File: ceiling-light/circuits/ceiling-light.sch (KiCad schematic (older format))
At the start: 55 parts, among them J1 Screw_Terminal_01x03, J2 Screw_Terminal_01x02, P1 ESProg_Mating_Header, Q1 IRF840, Q2 IRF840, Q3 KSP44, SW1 SW_Push, SW2 SW_Push, U1 TMP36xS, U2 FL51xxMX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

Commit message: schematic work
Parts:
- added Q? (x2): IRF840, Package_TO_SOT_SMD:TO-263-2_TabPin1, symbol Transistor_FET:IRF740
- added R17: 1M, Resistor_SMD:R_1210_3225Metric_Pad1.42x2.65mm_HandSolder, symbol Device:R_Small
- added R?: 10K, Resistor_SMD:R_1210_3225Metric_Pad1.42x2.65mm_HandSolder, symbol Device:R
- added U?: 4N35, Package_DIP:DIP-6_W7.62mm, symbol Isolator:4N35
- R8: value 2M2 -> 1M
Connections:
- net GND: now also U4.3, Q?.3 (S), Q?.3 (S), R?.2
- net at C3.1, D1.2 (A), J1.1 (Pin_1)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: now also C2.2, R17.2; no longer C2.1, R8.2
- net at F1.1, L2.1, Q1.2 (D)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: now also C2.1; no longer C2.2
- net at U6.37 (IO23): now also R12.2, U4.4; no longer U4.3
- new net: R17.1, R8.2
- new net: Q?.1 (G), Q?.1 (G), R?.1, U?.4
- new net +12V: U?.5
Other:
- note added: "!! MAINS VOLTAGE | 230VAC | NOT ISOLATED !!"
- note removed: "!! MAINS VOLTAGE | 230VAC !!"
- moved on the sheet: C1, C12, C13, C15, C2, C4, C6, D1, D2, L1, Q1, Q2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

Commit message: new design
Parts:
- removed C12: 4µ7, Capacitor_SMD:C_1206_3216Metric_Pad1.42x1.75mm_HandSolder, symbol Device:CP_Small
- removed C13: 0.1µ, Capacitor_SMD:C_1206_3216Metric_Pad1.42x1.75mm_HandSolder, symbol Device:CP_Small
- removed C15: 10µ, Capacitor_SMD:C_1210_3225Metric_Pad1.42x2.65mm_HandSolder, symbol Device:CP_Small
- removed D2: WS2812B, LED_SMD:LED_WS2812B_PLCC4_5.0x5.0mm_P3.2mm, symbol LED:WS2812B
- removed D3: LED, symbol Device:LED
- removed D4: D_Bridge_+-AA, Diode_THT_slimc:DB107-BP, symbol Device:D_Bridge_+-AA
- removed Q? (x2): IRF840, Package_TO_SOT_SMD:TO-263-2_TabPin1, symbol Transistor_FET:IRF740
- removed R14, R15: 1K, Resistor_SMD:R_1210_3225Metric_Pad1.42x2.65mm_HandSolder, symbol Device:R_Small
- removed R16: 10K, Resistor_SMD:R_1210_3225Metric_Pad1.42x2.65mm_HandSolder, symbol Device:R_Small
- removed R9: xx, symbol Device:R
- removed R?: 10K, Resistor_SMD:R_1210_3225Metric_Pad1.42x2.65mm_HandSolder, symbol Device:R
- removed U1: TMP36xS, Package_TO_SOT_SMD:SOT-23-5_HandSoldering, symbol Sensor_Temperature:TMP36xS
- removed U5: DAC081C081CIMK, Package_TO_SOT_SMD:SOT-23-6_Handsoldering, symbol Analog_DAC:DAC081C081CIMK
- removed U6: ESP32-WROOM-32D, RF_Module:ESP32-WROOM-32, symbol RF_Module:ESP32-WROOM-32D
- removed U?: 4N35, Package_DIP:DIP-6_W7.62mm, symbol Isolator:4N35
- added C11: 10µ, Capacitor_SMD:C_1210_3225Metric_Pad1.42x2.65mm_HandSolder, symbol Device:CP_Small
- added Q4: BSS138, Package_TO_SOT_SMD:SOT-23, symbol Transistor_FET:BSS138
- added R9: 10K, Resistor_SMD:R_1210_3225Metric_Pad1.42x2.65mm_HandSolder, symbol Device:R_Small
- added U5: ESP-12E, RF_Module:ESP-12E, symbol RF_Module:ESP-12E
- C1: value 0.1µ -> 100µF 16V
- C2, C3, C8: value 100n -> 100n 630V
- C6: value 0.1µ -> 47µF 25V; footprint Capacitor_SMD:C_1206_3216Metric_Pad1.42x1.75mm_HandSolder -> Capacitor_SMD:C_1210_3225Metric_Pad1.42x2.65mm_HandSolder
- R6: value 1K -> 1.2K
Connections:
- net +3V3: now also C11.1, Q4.1 (G), U5.8 (VCC); no longer C6.1, R11.1
- net +5V: now also R9.1
- net GND: now also C11.2, U5.15 (GND); no longer R6.2
- net at C2.2, C3.1, D1.2 (A)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: now also R13.2; no longer R10.2
- net at J1.2 (Pin_2): now also R10.2; no longer R13.2
- net at C1.1: now also R6.2, U2.2 (DIMCN)
- net ESP_IO0: now reaches R12.2, U4.4
- net ESP_IO0: now also C6.1, P1.2 (GPIO0), SW2.2, U5.18 (GPIO0)
- net at R6.1: now also Q4.3 (D), R9.2
- net at R13.1: now also U4.1
- net at U4.2: now also R10.1
- removed net ESP32_BOOT: P1.2 (GPIO0), R7.2, SW2.2
- net ESP32_RST renamed ESP_RST
- net ESP_RST: now also U5.1 (~RST)
- net ESP32_RXD renamed ESP_RXD
- net ESP_RXD: now also U5.21 (GPIO3/RXD)
- net ESP32_TXD renamed ESP_TXD
- net ESP_TXD: now also U5.22 (GPIO1/TXD)
- new net: R11.1, U5.7 (GPIO13)
- new net ESP_ADC0: U5.2 (ADC)
- new net ESP_EN: U5.3 (EN)
- new net ESP_IO2: Q4.2 (S), R7.2, U5.17 (GPIO2)
- no-connect marks 26 -> 12
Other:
- note added: "MAINS SWITCH SENSE"
- note removed: "!! MAINS VOLTAGE | 230VAC | NOT ISOLATED !!"
- note removed: "630V"
- note removed: "DAC (RAIL TO RAIL)"
- note removed: "MAINS SWITCH SENSE (ZERO CROSSING)"
- note removed: "PCB TEMP SENSOR"
- note removed: "STATUS LED"
- moved on the sheet: C10, C14, C2, C3, C4, C5, C7, C8, C9, D1, D5, F1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

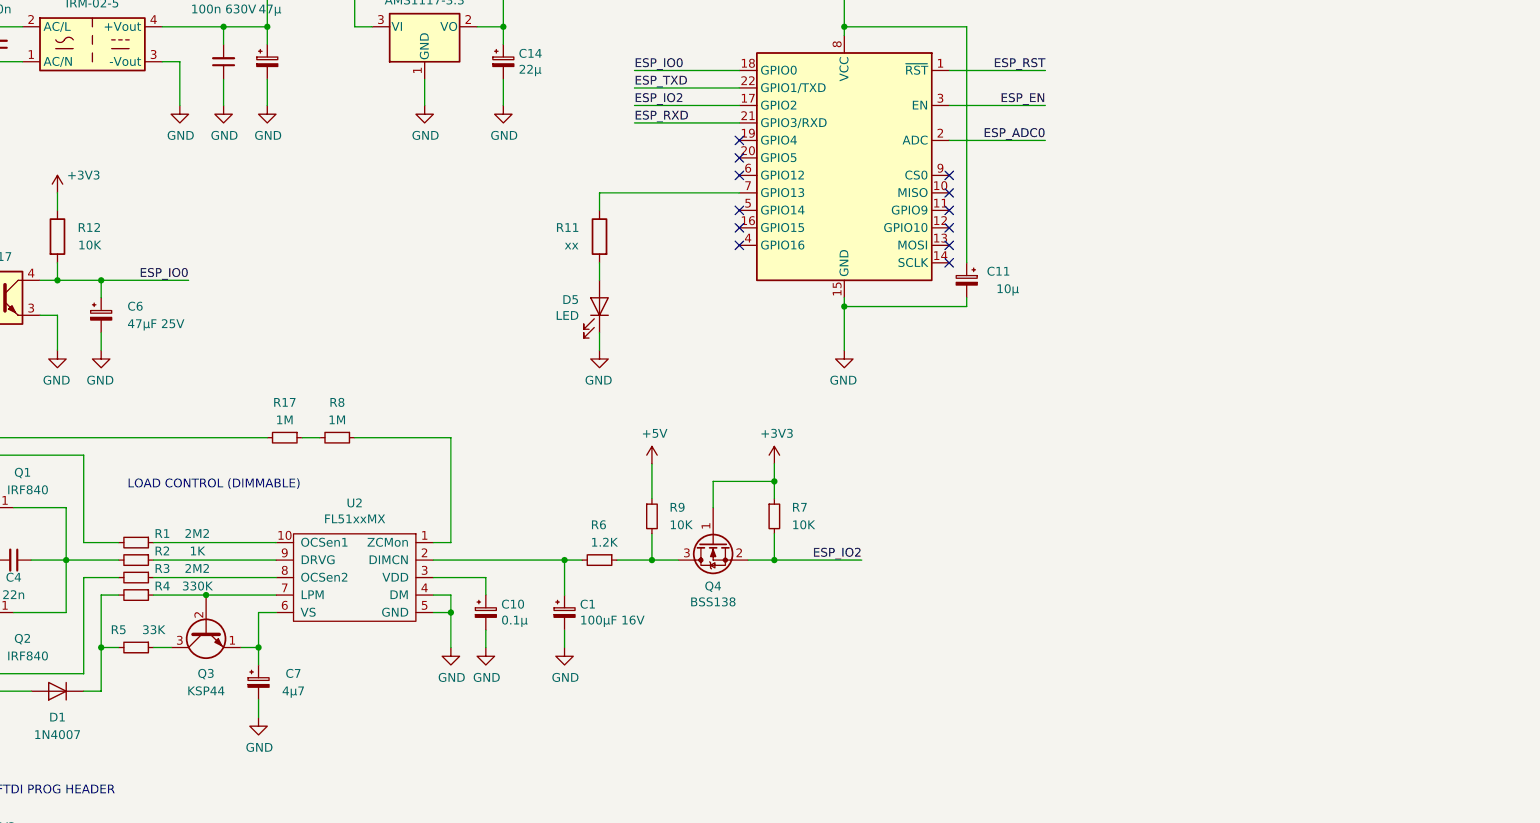
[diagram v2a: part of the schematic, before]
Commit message: adjusted component values
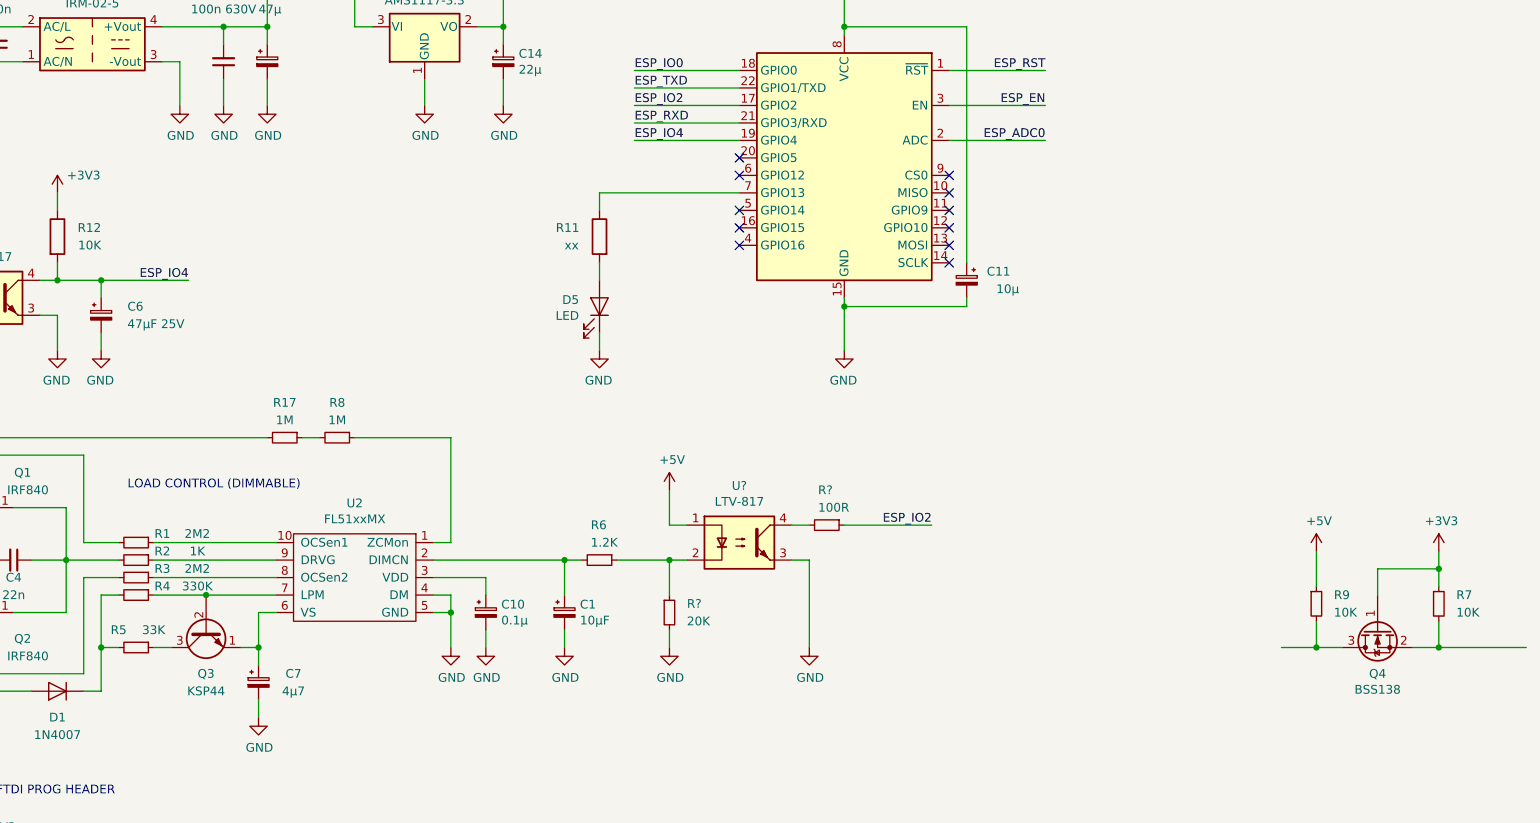
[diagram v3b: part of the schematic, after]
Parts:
- added R?: 20K, Resistor_SMD:R_1210_3225Metric_Pad1.42x2.65mm_HandSolder, symbol Device:R_Small
- added R?: 100R, Resistor_SMD:R_1210_3225Metric_Pad1.42x2.65mm_HandSolder, symbol Device:R_Small
- added U?: LTV-817, Package_DIP:SMDIP-4_W7.62mm, symbol Isolator:LTV-817
- C1: value 100µF 16V -> 10µF
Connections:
- net +5V: now also U?.1
- net ESP_IO0: no longer C6.1, R12.2, U4.4
- net ESP_IO2: now also R?.1; no longer Q4.2 (S), R7.2
- net GND: now also R?.2, U?.3
- net at Q4.3 (D), R9.2: no longer R6.1
- net ESP_IO4: now reaches U5.19 (GPIO4)
- net ESP_IO4: now also C6.1, R12.2, U4.4
- new net: Q4.2 (S), R7.2
- new net: R6.1, R?.1, U?.2
- new net: R?.2, U?.4
- no-connect marks 12 -> 11
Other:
- moved on the sheet: Q4, R7, R9
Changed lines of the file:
@@
 	1250 2900 1250 3800
-$Comp
-L Device:R_Small R9
-U 1 1 5DD78F51
-P 6450 4250
-F 0 "R9" H 6550 4300 50  0000 L CNN
-F 1 "10K" H 6550 4200 50  0000 L CNN
-F 2 "Resistor_SMD:R_1210_3225Metric_Pad1.42x2.65mm_HandSolder" H 6450 4250 50  0001 C CNN
-F 3 "~" H 6450 4250 50  0001 C CNN
-	1    6450 4250
-	1    0    0    -1
-$EndComp
 $Comp
 L power:+5V #PWR023
@@
 NoConn ~ 6950 2300
 NoConn ~ 6950 2200
-NoConn ~ 6950 2100
 Wire Wire Line
 	7550 3000 7550 3050
@@
 	7550 1450 7550 1500
 Text Label 3800 2900 2    50   ~ 0
-ESP_IO0
+ESP_IO4
 Wire Wire Line
 	3050 2900 3300 2900
@@
 Wire Wire Line
 	6350 1700 6950 1700
-$Comp
-L Transistor_FET:BSS138 Q4
-U 1 1 5D9B4897
-P 6800 4400
-F 0 "Q4" V 7050 4400 50  0000 C CNN
-F 1 "BSS138" V 7141 4400 50  0000 C CNN
-F 2 "Package_TO_SOT_SMD:SOT-23" H 7000 4325 50  0001 L CIN
-F 3 "https://www.fairchildsemi.com/datasheets/BS/BSS138.pdf" H 6800 4400 50  0001 L CNN
-	1    6800 4400
-	0    -1   1    0
-$EndComp
-$Comp
-L Device:R_Small R7
-U 1 1 5DA165F7
-P 7150 4250
-F 0 "R7" H 7250 4300 50  0000 L CNN
-F 1 "10K" H 7250 4200 50  0000 L CNN
-F 2 "Resistor_SMD:R_1210_3225Metric_Pad1.42x2.65mm_HandSolder" H 7150 4250 50  0001 C CNN
-F 3 "~" H 7150 4250 50  0001 C CNN
-	1    7150 4250
-	1    0    0    -1
-$EndComp
-Wire Wire Line
-	7150 4500 7150 4350
-Wire Wire Line
-	7000 4500 7150 4500
-Wire Wire Line
-	6450 4350 6450 4500
-Wire Wire Line
-	6450 4500 6600 4500
 $Comp
 L Device:R_Small R6
@@
 P 5950 4800
 F 0 "C1" H 6038 4846 50  0000 L CNN
-F 1 "100µF 16V" H 6038 4755 50  0000 L CNN
+F 1 "10µF" H 6038 4755 50  0000 L CNN
 F 2 "Capacitor_SMD:C_1206_3216Metric_Pad1.42x1.75mm_HandSolder" H 5950 4800 50  0001 C CNN
 F 3 "~" H 5950 4800 50  0001 C CNN
@@
 	5950 4500 5200 4500
 Connection ~ 5950 4500
-Wire Wire Line
-	6250 4500 6450 4500
-Connection ~ 6450 4500
 Text Label 6350 1900 0    50   ~ 0
 ESP_IO2
 Wire Wire Line
 	6350 1900 6950 1900
-Text Label 7650 4500 2    50   ~ 0
+Text Label 8050 4300 2    50   ~ 0
 ESP_IO2
-Wire Wire Line
-	7650 4500 7150 4500
-Connection ~ 7150 4500
+Text Label 6350 2100 0    50   ~ 0
+ESP_IO4
+Wire Wire Line
+	6350 2100 6950 2100
+$Comp
+L Isolator:LTV-817 U?
+U 1 1 5D9C73D3
+P 6950 4400
+F 0 "U?" H 6950 4725 50  0000 C CNN
+F 1 "LTV-817" H 6950 4634 50  0000 C CNN
+F 2 "Package_DIP:SMDIP-4_W7.62mm" H 6750 4200 50  0001 L CIN
+F 3 "http://www.us.liteon.com/downloads/LTV-817-827-847.PDF" H 6950 4300 50  0001 L CNN
+	1    6950 4400
+	1    0    0    -1
+$EndComp
+Wire Wire Line
+	6250 4500 6550 4500
+$Comp
+L Device:R_Small R?
+U 1 1 5D9E5728
+P 6550 4800
+F 0 "R?" H 6650 4850 50  0000 L CNN
+F 1 "20K" H 6650 4750 50  0000 L CNN
+F 2 "Resistor_SMD:R_1210_3225Metric_Pad1.42x2.65mm_HandSolder" H 6550 4800 50  0001 C CNN
+F 3 "~" H 6550 4800 50  0001 C CNN
+	1    6550 4800
+	1    0    0    -1
+$EndComp
+Wire Wire Line
+	6550 4700 6550 4500
+Connection ~ 6550 4500
+Wire Wire Line
+	6550 4500 6650 4500
+$Comp
+L power:GND #PWR?
+U 1 1 5D9F7709
+P 6550 5000
+F 0 "#PWR?" H 6550 4750 50  0001 C CNN
+F 1 "GND" H 6555 4827 50  0000 C CNN
+F 2 "" H 6550 5000 50  0001 C CNN
+F 3 "" H 6550 5000 50  0001 C CNN
+	1    6550 5000
+	1    0    0    -1
+$EndComp
+Wire Wire Line
+	6550 5000 6550 4900
+$Comp
+L power:+5V #PWR?
+U 1 1 5D9FDF1B
+P 6550 4100
+F 0 "#PWR?" H 6550 3950 50  0001 C CNN
+F 1 "+5V" H 6565 4273 50  0000 C CNN
+F 2 "" H 6550 4100 50  0001 C CNN
+F 3 "" H 6550 4100 50  0001 C CNN
+	1    6550 4100
+	1    0    0    -1
+$EndComp
+Wire Wire Line
+	6650 4300 6550 4300
+Wire Wire Line
+	6550 4300 6550 4100
+$Comp
+L power:GND #PWR?
+U 1 1 5DA0AEB1
+P 7350 5000
+F 0 "#PWR?" H 7350 4750 50  0001 C CNN
+F 1 "GND" H 7355 4827 50  0000 C CNN
+F 2 "" H 7350 5000 50  0001 C CNN
+F 3 "" H 7350 5000 50  0001 C CNN
+	1    7350 5000
+	1    0    0    -1
+$EndComp
+Wire Wire Line
+	7250 4500 7350 4500
+Wire Wire Line
+	7350 4500 7350 5000
+$Comp
+L Device:R_Small R?
+U 1 1 5DA17ECE
+P 7450 4300
+F 0 "R?" V 7250 4250 50  0000 L CNN
+F 1 "100R" V 7350 4250 50  0000 L CNN
+F 2 "Resistor_SMD:R_1210_3225Metric_Pad1.42x2.65mm_HandSolder" H 7450 4300 50  0001 C CNN
+F 3 "~" H 7450 4300 50  0001 C CNN
+	1    7450 4300
+	0    1    1    0
+$EndComp
+Wire Wire Line
+	7250 4300 7350 4300
+Wire Wire Line
+	7550 4300 8050 4300
+Wire Wire Line
+	10950 4550 10950 4450
+Wire Wire Line
+	10600 4550 10950 4550
+Wire Wire Line
+	10600 4700 10600 4550
+Wire Wire Line
+	10250 4450 10250 4650
+$Comp
+L power:+5V #PWR0106
+U 1 1 5DA7EE62
+P 10250 4450
+F 0 "#PWR0106" H 10250 4300 50  0001 C CNN
+F 1 "+5V" H 10265 4623 50  0000 C CNN
+F 2 "" H 10250 4450 50  0001 C CNN
+F 3 "" H 10250 4450 50  0001 C CNN
+	1    10250 4450
+	1    0    0    -1
+$EndComp
+Connection ~ 10950 4550
+Wire Wire Line
+	10950 4650 10950 4550
 $Comp
 L power:+3V3 #PWR0105
 U 1 1 5DA78E33
-P 7150 3950
-F 0 "#PWR0105" H 7150 3800 50  0001 C CNN
-F 1 "+3V3" H 7165 4123 50  0000 C CNN
-F 2 "" H 7150 3950 50  0001 C CNN
-F 3 "" H 7150 3950 50  0001 C CNN
-	1    7150 3950
-	1    0    0    -1
-$EndComp
-Wire Wire Line
-	7150 4150 7150 4050
-$Comp
-L power:+5V #PWR0106
-U 1 1 5DA7EE62
-P 6450 3950
-F 0 "#PWR0106" H 6450 3800 50  0001 C CNN
-F 1 "+5V" H 6465 4123 50  0000 C CNN
-F 2 "" H 6450 3950 50  0001 C CNN
-F 3 "" H 6450 3950 50  0001 C CNN
-	1    6450 3950
-	1    0    0    -1
-$EndComp
-Wire Wire Line
-	6450 3950 6450 4150
-Wire Wire Line
-	6800 4200 6800 4050
-Wire Wire Line
-	6800 4050 7150 4050
-Connection ~ 7150 4050
-Wire Wire Line
-	7150 4050 7150 3950
+P 10950 4450
+F 0 "#PWR0105" H 10950 4300 50  0001 C CNN
+F 1 "+3V3" H 10965 4623 50  0000 C CNN
+F 2 "" H 10950 4450 50  0001 C CNN
+F 3 "" H 10950 4450 50  0001 C CNN
+	1    10950 4450
+	1    0    0    -1
+$EndComp
+Wire Wire Line
+	10050 5000 10250 5000
+Wire Wire Line
+	10250 5000 10400 5000
+Connection ~ 10250 5000
+Wire Wire Line
+	10250 4850 10250 5000
+Wire Wire Line
+	11450 5000 10950 5000
+Wire Wire Line
+	10800 5000 10950 5000
+Connection ~ 10950 5000
+Wire Wire Line
+	10950 5000 10950 4850
+$Comp
+L Device:R_Small R7
+U 1 1 5DA165F7
+P 10950 4750
+F 0 "R7" H 11050 4800 50  0000 L CNN
+F 1 "10K" H 11050 4700 50  0000 L CNN
+F 2 "Resistor_SMD:R_1210_3225Metric_Pad1.42x2.65mm_HandSolder" H 10950 4750 50  0001 C CNN
+F 3 "~" H 10950 4750 50  0001 C CNN
+	1    10950 4750
+	1    0    0    -1
+$EndComp
+$Comp
+L Transistor_FET:BSS138 Q4
+U 1 1 5D9B4897
+P 10600 4900
+F 0 "Q4" V 10850 4900 50  0000 C CNN
+F 1 "BSS138" V 10941 4900 50  0000 C CNN
+F 2 "Package_TO_SOT_SMD:SOT-23" H 10800 4825 50  0001 L CIN
+F 3 "https://www.fairchildsemi.com/datasheets/BS/BSS138.pdf" H 10600 4900 50  0001 L CNN
+	1    10600 4900
+	0    -1   1    0
+$EndComp
+$Comp
+L Device:R_Small R9
+U 1 1 5DD78F51
+P 10250 4750
+F 0 "R9" H 10350 4800 50  0000 L CNN
+F 1 "10K" H 10350 4700 50  0000 L CNN
+F 2 "Resistor_SMD:R_1210_3225Metric_Pad1.42x2.65mm_HandSolder" H 10250 4750 50  0001 C CNN
+F 3 "~" H 10250 4750 50  0001 C CNN
+	1    10250 4750
+	1    0    0    -1
+$EndComp
 $EndSCHEMATC
